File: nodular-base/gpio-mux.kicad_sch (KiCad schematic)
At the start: 0 parts

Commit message: WIP layout for base
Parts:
- added U24, U25, U26: AW9523B, Package_DFN_QFN:QFN-24-1EP_4x4mm_P0.5mm_EP2.7x2.6mm, symbol nodular:AW9523B
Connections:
- new net 3V3_SYS: U24.21 (VCC), U25.18 (AD0), U25.21 (VCC), U26.21 (VCC), U26.24 (AD1)
- new net ALS1: U26.8 (P0_3)
- new net ALS2: U26.1 (P1_0)
- new net ALS3: U26.2 (P1_1)
- new net ALS4: U26.3 (P1_2)
- new net ALS5: U26.4 (P1_3)
- new net BLS1: U26.5 (P0_0)
- new net BLS2: U26.6 (P0_1)
- new net BLS3: U25.15 (P1_5)
- new net BLS4: U25.16 (P1_6)
- new net BLS5: U25.17 (P1_7)
- new net BTN1: U26.12 (P0_6)
- new net BTN2: U26.13 (P0_7)
- new net BTN3: U25.5 (P0_0)
- new net BTN4: U25.6 (P0_1)
- new net BTN5: U25.7 (P0_2)
- new net BTN6: U25.8 (P0_3)
- new net CAN_EN: U26.10 (P0_4)
- new net CLS1: U25.10 (P0_4)
- new net CLS2: U25.11 (P0_5)
- new net CLS3: U25.12 (P0_6)
- new net CLS4: U25.13 (P0_7)
- new net CLS5: U25.14 (P1_4)
- new net DET_A: U26.14 (P1_4)
- new net DET_B: U26.15 (P1_5)
- new net DET_C: U25.1 (P1_0)
- new net DET_D: U25.2 (P1_1)
- new net DET_E: U25.3 (P1_2)
- new net DET_F: U25.4 (P1_3)
- new net DLS1: U24.1 (P1_0)
- new net DLS2: U24.2 (P1_1)
- new net DLS3: U24.3 (P1_2)
- new net DLS4: U24.4 (P1_3)
- new net DLS5: U24.5 (P0_0)
- new net ELS1: U24.7 (P0_2)
- new net ELS2: U24.8 (P0_3)
- new net ELS3: U24.10 (P0_4)
- new net ELS4: U24.11 (P0_5)
- new net ELS5: U24.12 (P0_6)
- new net FLS1: U24.13 (P0_7)
- new net FLS2: U24.14 (P1_4)
- new net FLS3: U24.15 (P1_5)
- new net FLS4: U24.16 (P1_6)
- new net FLS5: U24.17 (P1_7)
- new net GND: U24.18 (AD0), U24.24 (AD1), U24.25 (GND), U24.9 (GND), U25.24 (AD1), U25.25 (GND), U25.9 (GND), U26.18 (AD0), U26.25 (GND), U26.9 (GND)
- new net LED_PWR_EN: U26.7 (P0_2)
- new net SCL_SYS: U24.19 (SCL), U25.19 (SCL), U26.19 (SCL)
- new net SDA_SYS: U24.20 (SDA), U25.20 (SDA), U26.20 (SDA)
- new net ~{INT_SYS}: U24.22 (~{INT}), U25.22 (~{INT}), U26.22 (~{INT})

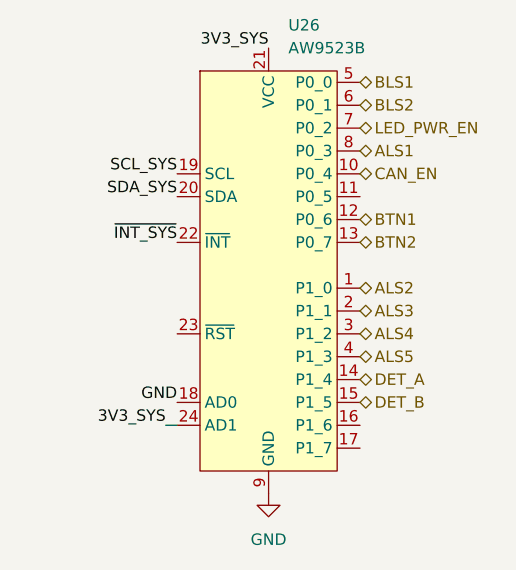
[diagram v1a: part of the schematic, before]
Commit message: Switched from CAN to USB for second USB-C port Added second PD controller and USB mux to allow switching between host and device port Added SOICbite to corner All routing complete Updated pin map, added i2c addresses, soicbit pin mapping, and fpc pinout to document
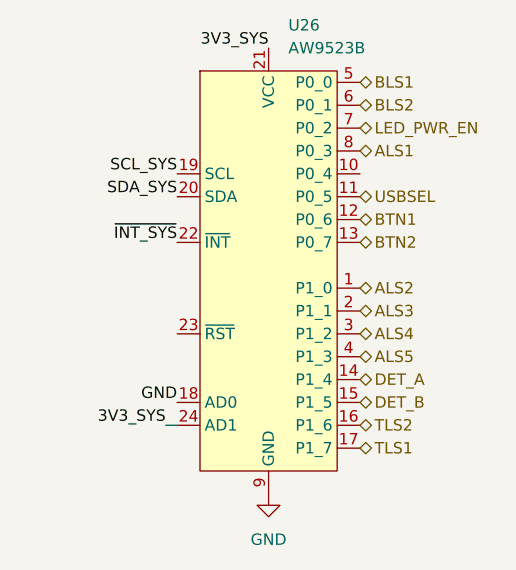
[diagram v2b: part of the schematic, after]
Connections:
- net USBSEL: now reaches U26.11 (P0_5)
- net TLS2: now reaches U26.16 (P1_6)
- net TLS1: now reaches U26.17 (P1_7)
- net CAN_EN: no longer names the net of U26.10 (P0_4)
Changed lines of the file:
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@@
+    (effects (font (size 1.27 1.27)) (justify left))
+  )
+  (hierarchical_label "USBSEL" (shape bidirectional) (at 205.74 77.47 0) (fields_autoplaced)
+    (effects (font (size 1.27 1.27)) (justify left))
+  )
+  (hierarchical_label "TLS1" (shape bidirectional) (at 205.74 105.41 0) (fields_autoplaced)
     (effects (font (size 1.27 1.27)) (justify left))
   )
@@
   (hierarchical_label "SCL_SYS" (shape input) (at 59.69 60.96 180) (fields_autoplaced)
     (effects (font (size 1.27 1.27)) (justify right))
-  )
-  (hierarchical_label "CAN_EN" (shape bidirectional) (at 205.74 74.93 0) (fields_autoplaced)
-    (effects (font (size 1.27 1.27)) (justify left))
   )
   (hierarchical_label "BLS5" (shape bidirectional) (at 156.21 105.41 0) (fields_autoplaced)
@@
     (effects (font (size 1.27 1.27)) (justify left))
   )
+  (hierarchical_label "TLS2" (shape bidirectional) (at 205.74 102.87 0) (fields_autoplaced)
+    (effects (font (size 1.27 1.27)) (justify left))
+  )

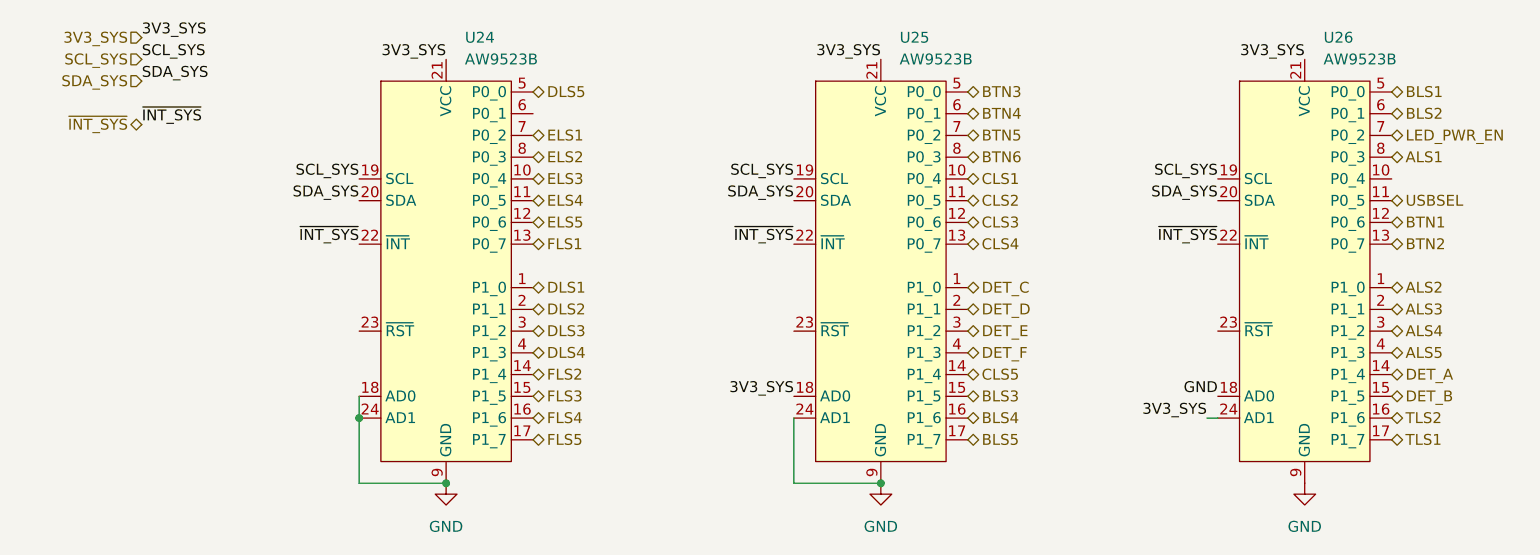
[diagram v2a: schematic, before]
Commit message: Add hole Add decoupling caps, pullups, and voltage dividers Set current limit on PMIC Determine battery attachment angle Update BOM and pinouts
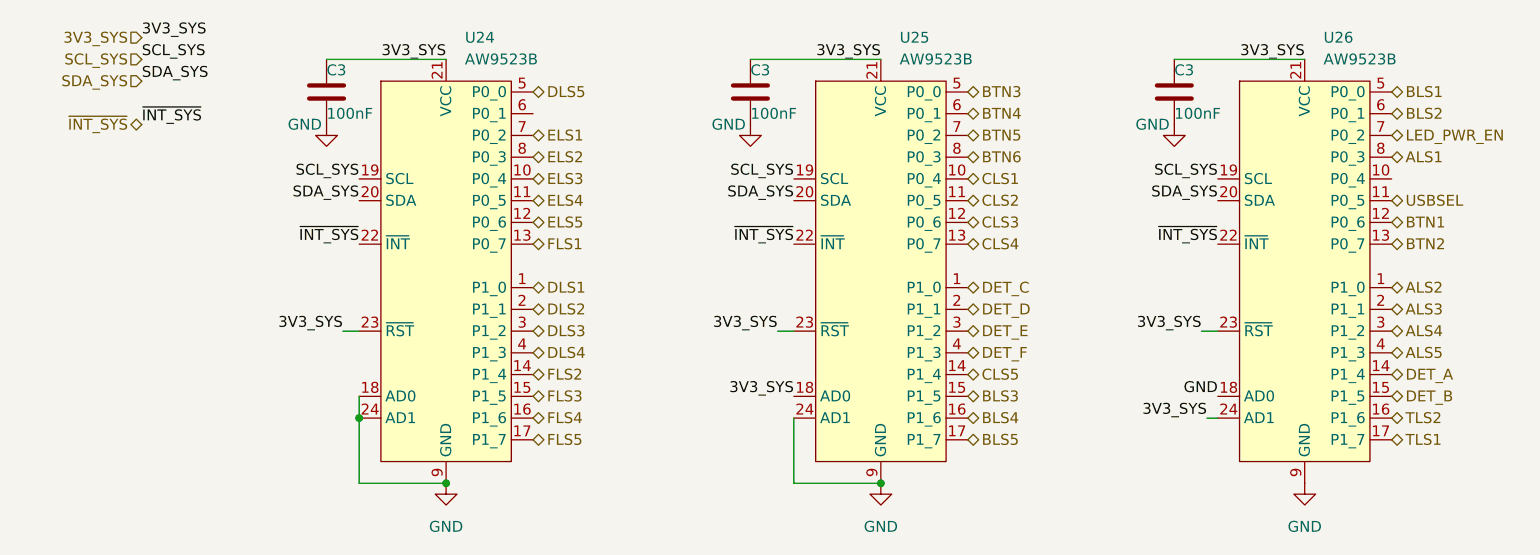
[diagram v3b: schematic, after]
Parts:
- added C3 (x3): 100nF, Capacitor_SMD:C_0402_1005Metric, symbol Device:C
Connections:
- net 3V3_SYS: now also U24.23 (~{RST}), U25.23 (~{RST}), U26.23 (~{RST}), C3.1, C3.1, C3.1
- net GND: now also C3.2, C3.2, C3.2
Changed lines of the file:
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@@
+    (stroke (width 0) (type default))
+  )
+  (wire (pts (xy 183.515 92.71) (xy 185.42 92.71))
     (stroke (width 0) (type default))
   )
@@
     (stroke (width 0) (type default))
   )
+  (wire (pts (xy 180.34 60.96) (xy 195.58 60.96))
+    (stroke (width 0) (type default))
+  )
   (wire (pts (xy 85.09 102.87) (xy 85.09 100.33))
     (stroke (width 0) (type default))
   )
+  (wire (pts (xy 130.81 60.96) (xy 146.05 60.96))
+    (stroke (width 0) (type default))
+  )
   (wire (pts (xy 184.15 102.87) (xy 185.42 102.87))
     (stroke (width 0) (type default))
   )
+  (wire (pts (xy 133.985 92.71) (xy 135.89 92.71))
+    (stroke (width 0) (type default))
+  )
+  (wire (pts (xy 83.185 92.71) (xy 85.09 92.71))
+    (stroke (width 0) (type default))
+  )
   (wire (pts (xy 95.25 110.49) (xy 85.09 110.49))
     (stroke (width 0) (type default))
   )
   (wire (pts (xy 135.89 102.87) (xy 135.89 110.49))
+    (stroke (width 0) (type default))
+  )
+  (wire (pts (xy 81.28 60.96) (xy 95.25 60.96))
     (stroke (width 0) (type default))
   )
@@
     (effects (font (size 1.27 1.27)) (justify right bottom))
   )
+  (label "3V3_SYS" (at 83.185 92.71 180) (fields_autoplaced)
+    (effects (font (size 1.27 1.27)) (justify right bottom))
+  )
   (label "3V3_SYS" (at 146.05 60.96 180) (fields_autoplaced)
     (effects (font (size 1.27 1.27)) (justify right bottom))
   )
   (label "3V3_SYS" (at 184.15 102.87 180) (fields_autoplaced)
+    (effects (font (size 1.27 1.27)) (justify right bottom))
+  )
+  (label "3V3_SYS" (at 133.985 92.71 180) (fields_autoplaced)
     (effects (font (size 1.27 1.27)) (justify right bottom))
   )
@@
     (effects (font (size 1.27 1.27)) (justify left bottom))
   )
+  (label "3V3_SYS" (at 183.515 92.71 180) (fields_autoplaced)
+    (effects (font (size 1.27 1.27)) (justify right bottom))
+  )
   (label "SDA_SYS" (at 135.89 77.47 180) (fields_autoplaced)
     (effects (font (size 1.27 1.27)) (justify right bottom))
@@
   (hierarchical_label "DLS1" (shape bidirectional) (at 105.41 87.63 0) (fields_autoplaced)
     (effects (font (size 1.27 1.27)) (justify left))
+  )
+  (symbol (lib_id "Device:C") (at 180.34 64.77 0) (unit 1)
+    (in_bom yes) (on_board yes) (dnp no)
+    (property "Reference" "C3" (at 180.34 62.23 0)
+      (effects (font (size 1.27 1.27)) (justify left))
+    )
+    (property "Value" "100nF" (at 180.34 67.31 0)
+      (effects (font (size 1.27 1.27)) (justify left))
+    )
+    (property "Footprint" "Capacitor_SMD:C_0402_1005Metric" (at 181.3052 68.58 0)
+      (effects (font (size 1.27 1.27)) hide)
+    )
+    (property "Datasheet" "~" (at 180.34 64.77 0)
+      (effects (font (size 1.27 1.27)) hide)
+    )
+    (pin "1")
+    (pin "2")
+    (instances
+      (project "nodular-base"
+        (path "/6dcb0502-87e2-4c28-9ce8-81aab8925f06"
+          (reference "C3") (unit 1)
+        )
+        (path "/6dcb0502-87e2-4c28-9ce8-81aab8925f06/5ae693f9-48f3-406c-bbdf-b76d81cc71eb"
+          (reference "C16") (unit 1)
+        )
+        (path "/6dcb0502-87e2-4c28-9ce8-81aab8925f06/52c49487-f3d5-40e2-8f19-e7b81498d838"
+          (reference "C45") (unit 1)
+        )
+      )
+    )
+  )
+  (symbol (lib_id "power:GND") (at 180.34 68.58 0) (unit 1)
+    (in_bom yes) (on_board yes) (dnp no)
+    (property "Reference" "#PWR065" (at 180.34 74.93 0)
+      (effects (font (size 1.27 1.27)) hide)
+    )
+    (property "Value" "GND" (at 177.8 68.58 0)
+      (effects (font (size 1.27 1.27)))
+    )
+    (property "Footprint" "" (at 180.34 68.58 0)
+      (effects (font (size 1.27 1.27)) hide)
+    )
+    (property "Datasheet" "" (at 180.34 68.58 0)
+      (effects (font (size 1.27 1.27)) hide)
+    )
+    (pin "1")
+    (instances
+      (project "nodular-base"
+        (path "/6dcb0502-87e2-4c28-9ce8-81aab8925f06/52c49487-f3d5-40e2-8f19-e7b81498d838"
+          (reference "#PWR065") (unit 1)
+        )
+      )
+    )
   )
   (symbol (lib_id "power:GND") (at 95.25 110.49 0) (unit 1)
@@
     )
   )
+  (symbol (lib_id "Device:C") (at 130.81 64.77 0) (unit 1)
+    (in_bom yes) (on_board yes) (dnp no)
+    (property "Reference" "C3" (at 130.81 62.23 0)
+      (effects (font (size 1.27 1.27)) (justify left))
+    )
+    (property "Value" "100nF" (at 130.81 67.31 0)
+      (effects (font (size 1.27 1.27)) (justify left))
+    )
+    (property "Footprint" "Capacitor_SMD:C_0402_1005Metric" (at 131.7752 68.58 0)
+      (effects (font (size 1.27 1.27)) hide)
+    )
+    (property "Datasheet" "~" (at 130.81 64.77 0)
+      (effects (font (size 1.27 1.27)) hide)
+    )
+    (pin "1")
+    (pin "2")
+    (instances
+      (project "nodular-base"
+        (path "/6dcb0502-87e2-4c28-9ce8-81aab8925f06"
+          (reference "C3") (unit 1)
+        )
+        (path "/6dcb0502-87e2-4c28-9ce8-81aab8925f06/5ae693f9-48f3-406c-bbdf-b76d81cc71eb"
+          (reference "C16") (unit 1)
+        )
+        (path "/6dcb0502-87e2-4c28-9ce8-81aab8925f06/52c49487-f3d5-40e2-8f19-e7b81498d838"
+          (reference "C44") (unit 1)
+        )
+      )
+    )
+  )
+  (symbol (lib_id "power:GND") (at 130.81 68.58 0) (unit 1)
+    (in_bom yes) (on_board yes) (dnp no)
+    (property "Reference" "#PWR064" (at 130.81 74.93 0)
+      (effects (font (size 1.27 1.27)) hide)
+    )
+    (property "Value" "GND" (at 128.27 68.58 0)
+      (effects (font (size 1.27 1.27)))
+    )
+    (property "Footprint" "" (at 130.81 68.58 0)
+      (effects (font (size 1.27 1.27)) hide)
+    )
+    (property "Datasheet" "" (at 130.81 68.58 0)
+      (effects (font (size 1.27 1.27)) hide)
+    )
+    (pin "1")
+    (instances
+      (project "nodular-base"
+        (path "/6dcb0502-87e2-4c28-9ce8-81aab8925f06/52c49487-f3d5-40e2-8f19-e7b81498d838"
+          (reference "#PWR064") (unit 1)
+        )
+      )
+    )
+  )
   (symbol (lib_id "nodular:AW9523B") (at 195.58 85.09 0) (unit 1)
     (in_bom yes) (on_board yes) (dnp no) (fields_autoplaced)
@@
         )
       )
+    )
+  )
+  (symbol (lib_id "Device:C") (at 81.28 64.77 0) (unit 1)
+    (in_bom yes) (on_board yes) (dnp no)
+    (property "Reference" "C3" (at 81.28 62.23 0)
+      (effects (font (size 1.27 1.27)) (justify left))
+    )
+    (property "Value" "100nF" (at 81.28 67.31 0)
+      (effects (font (size 1.27 1.27)) (justify left))
+    )
+    (property "Footprint" "Capacitor_SMD:C_0402_1005Metric" (at 82.2452 68.58 0)
+      (effects (font (size 1.27 1.27)) hide)
+    )
+    (property "Datasheet" "~" (at 81.28 64.77 0)
+      (effects (font (size 1.27 1.27)) hide)
+    )
+    (pin "1")
+    (pin "2")
+    (instances
+      (project "nodular-base"
+        (path "/6dcb0502-87e2-4c28-9ce8-81aab8925f06"
+          (reference "C3") (unit 1)
+        )
+        (path "/6dcb0502-87e2-4c28-9ce8-81aab8925f06/5ae693f9-48f3-406c-bbdf-b76d81cc71eb"
+          (reference "C16") (unit 1)
+        )
+        (path "/6dcb0502-87e2-4c28-9ce8-81aab8925f06/52c49487-f3d5-40e2-8f19-e7b81498d838"
+          (reference "C43") (unit 1)
+        )
+      )
+    )
+  )
+  (symbol (lib_id "power:GND") (at 81.28 68.58 0) (unit 1)
+    (in_bom yes) (on_board yes) (dnp no)
+    (property "Reference" "#PWR063" (at 81.28 74.93 0)
+      (effects (font (size 1.27 1.27)) hide)
+    )
+    (property "Value" "GND" (at 78.74 68.58 0)
+      (effects (font (size 1.27 1.27)))
+    )
+    (property "Footprint" "" (at 81.28 68.58 0)
+      (effects (font (size 1.27 1.27)) hide)
+    )
+    (property "Datasheet" "" (at 81.28 68.58 0)
+      (effects (font (size 1.27 1.27)) hide)
+    )
+    (pin "1")
+    (instances
+      (project "nodular-base"
+        (path "/6dcb0502-87e2-4c28-9ce8-81aab8925f06/52c49487-f3d5-40e2-8f19-e7b81498d838"
+          (reference "#PWR063") (unit 1)
+        )
+      )

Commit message: Add VCONN support and load switch with 1.5A current limit on host port Add accelerometer interrupt connection Update BOM with important capacitor and inductor PNs and costings
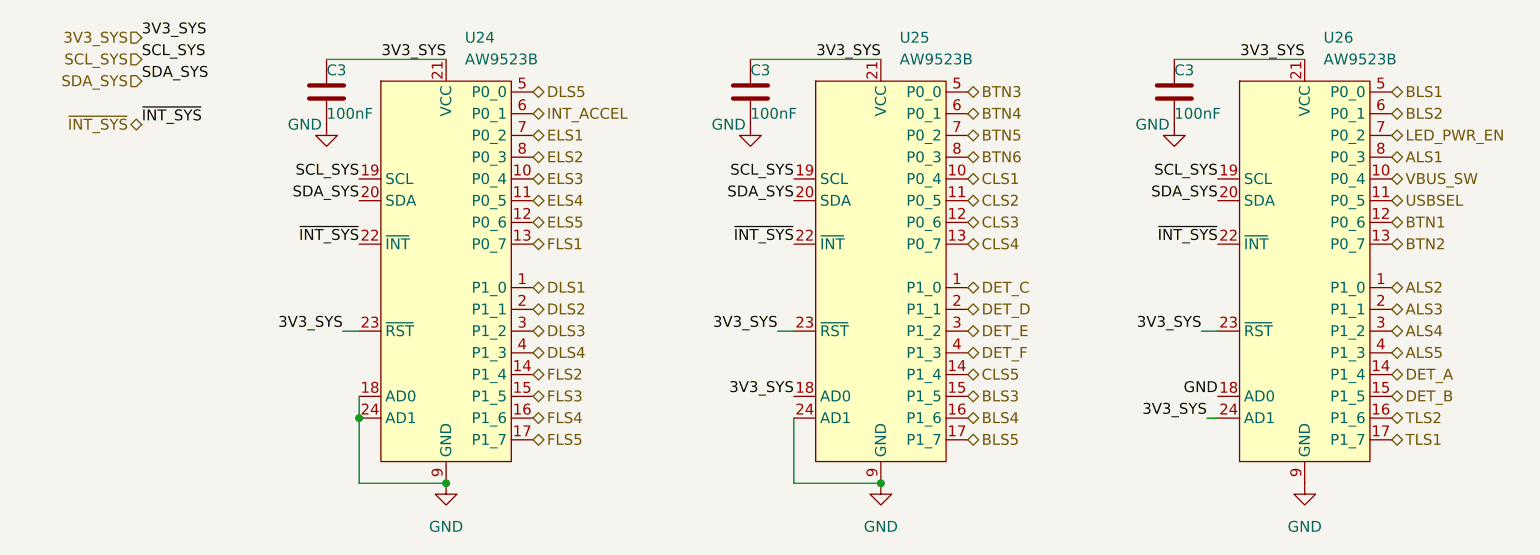
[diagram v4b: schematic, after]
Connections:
- net VBUS_SW: now reaches U26.10 (P0_4)
- net INT_ACCEL: now reaches U24.6 (P0_1)
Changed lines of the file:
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@@
+    (effects (font (size 1.27 1.27)) (justify left))
+  )
+  (hierarchical_label "INT_ACCEL" (shape bidirectional) (at 105.41 67.31 0) (fields_autoplaced)
     (effects (font (size 1.27 1.27)) (justify left))
   )
@@
     (effects (font (size 1.27 1.27)) (justify left))
   )
+  (hierarchical_label "VBUS_SW" (shape bidirectional) (at 205.74 74.93 0) (fields_autoplaced)
+    (effects (font (size 1.27 1.27)) (justify left))
+  )

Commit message: Add additional accelerometer-gyro option, update pin and address map, fix some ERC errors
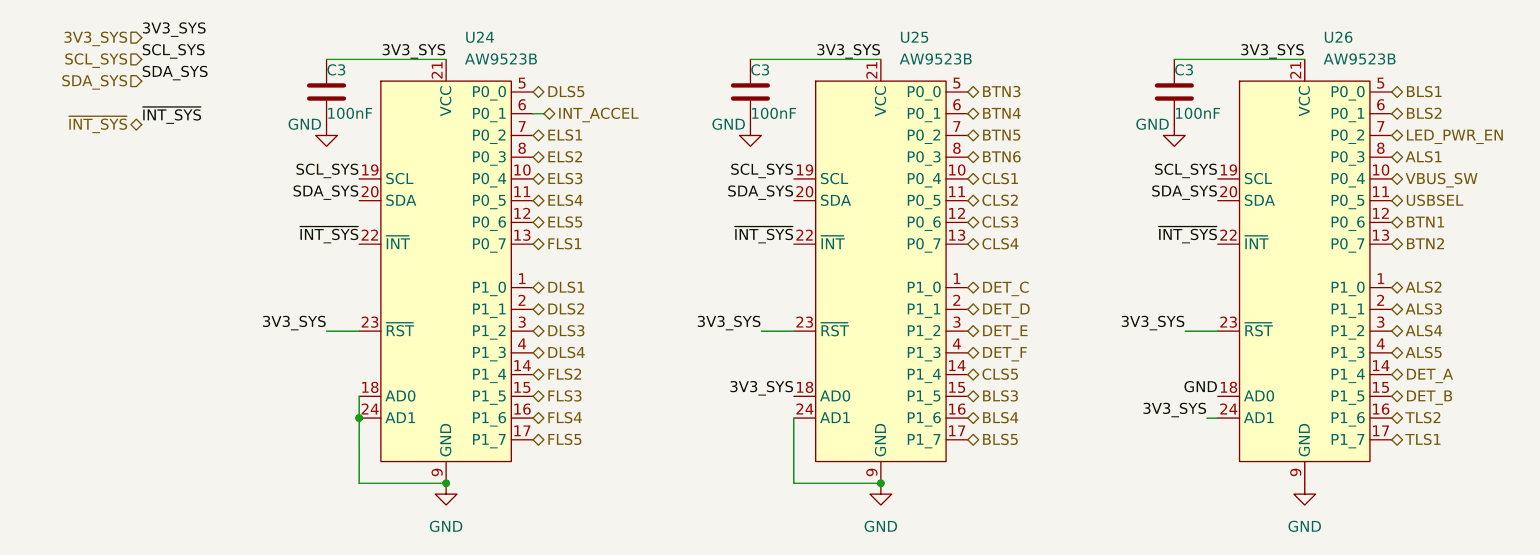
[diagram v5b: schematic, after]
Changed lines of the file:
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@@
     (stroke (width 0) (type default))
   )
-  (wire (pts (xy 183.515 92.71) (xy 185.42 92.71))
+  (wire (pts (xy 181.61 92.71) (xy 185.42 92.71))
     (stroke (width 0) (type default))
   )
@@
     (stroke (width 0) (type default))
   )
-  (wire (pts (xy 133.985 92.71) (xy 135.89 92.71))
+  (wire (pts (xy 132.08 92.71) (xy 135.89 92.71))
     (stroke (width 0) (type default))
   )
-  (wire (pts (xy 83.185 92.71) (xy 85.09 92.71))
+  (wire (pts (xy 81.28 92.71) (xy 85.09 92.71))
     (stroke (width 0) (type default))
   )
   (wire (pts (xy 95.25 110.49) (xy 85.09 110.49))
+    (stroke (width 0) (type default))
+  )
+  (wire (pts (xy 106.68 67.31) (xy 105.41 67.31))
     (stroke (width 0) (type default))
   )
@@
     (effects (font (size 1.27 1.27)) (justify right bottom))
   )
-  (label "3V3_SYS" (at 83.185 92.71 180) (fields_autoplaced)
+  (label "3V3_SYS" (at 81.28 92.71 180) (fields_autoplaced)
     (effects (font (size 1.27 1.27)) (justify right bottom))
   )
@@
     (effects (font (size 1.27 1.27)) (justify right bottom))
   )
-  (label "3V3_SYS" (at 133.985 92.71 180) (fields_autoplaced)
+  (label "3V3_SYS" (at 132.08 92.71 180) (fields_autoplaced)
     (effects (font (size 1.27 1.27)) (justify right bottom))
   )
@@
     (effects (font (size 1.27 1.27)) (justify left bottom))
   )
-  (label "3V3_SYS" (at 183.515 92.71 180) (fields_autoplaced)
+  (label "3V3_SYS" (at 181.61 92.71 180) (fields_autoplaced)
     (effects (font (size 1.27 1.27)) (justify right bottom))
   )
@@
     (effects (font (size 1.27 1.27)) (justify left))
   )
-  (hierarchical_label "INT_ACCEL" (shape bidirectional) (at 105.41 67.31 0) (fields_autoplaced)
+  (hierarchical_label "INT_ACCEL" (shape bidirectional) (at 106.68 67.31 0) (fields_autoplaced)
     (effects (font (size 1.27 1.27)) (justify left))
   )
